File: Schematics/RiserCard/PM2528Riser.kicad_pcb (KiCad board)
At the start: 2 copper layers, 116.5 x 105 mm, 64 parts, among them K2 Conn_02x40_Odd_Even

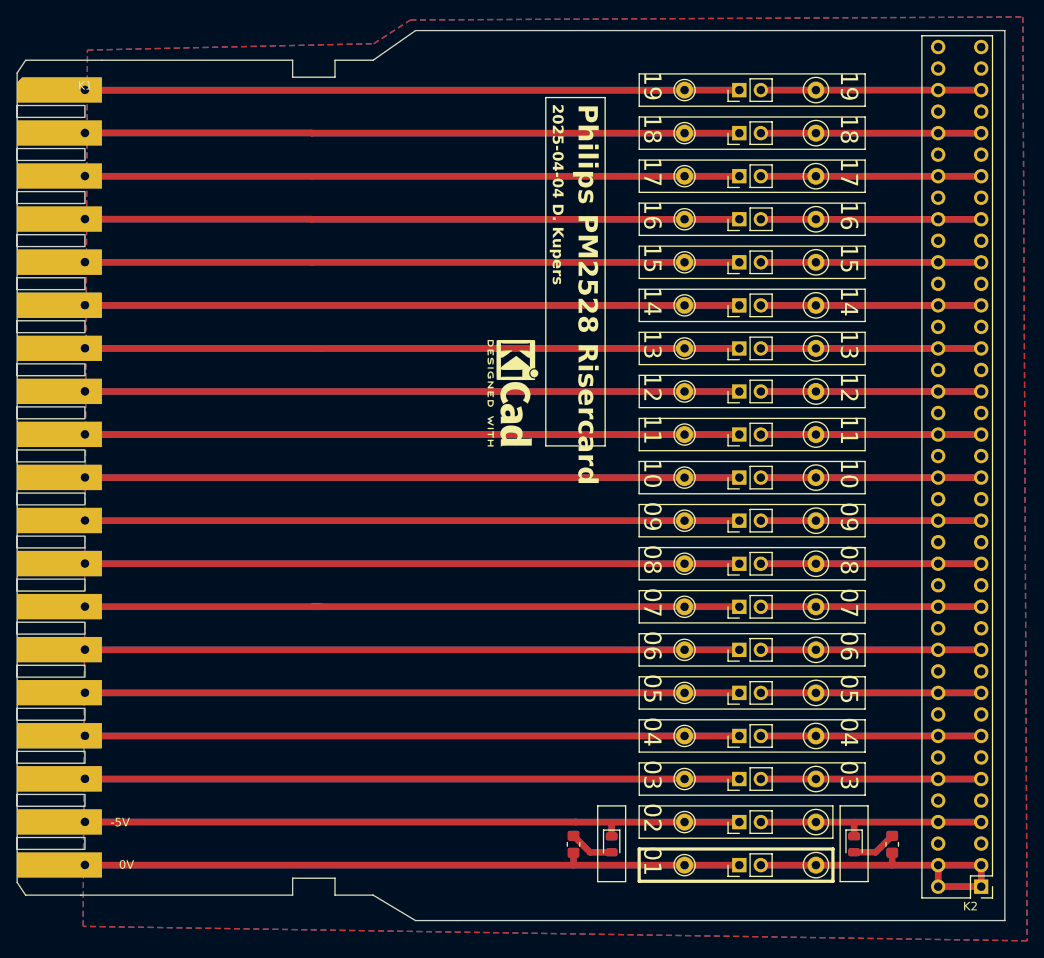
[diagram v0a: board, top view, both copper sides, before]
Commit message: Reworked N20/N21
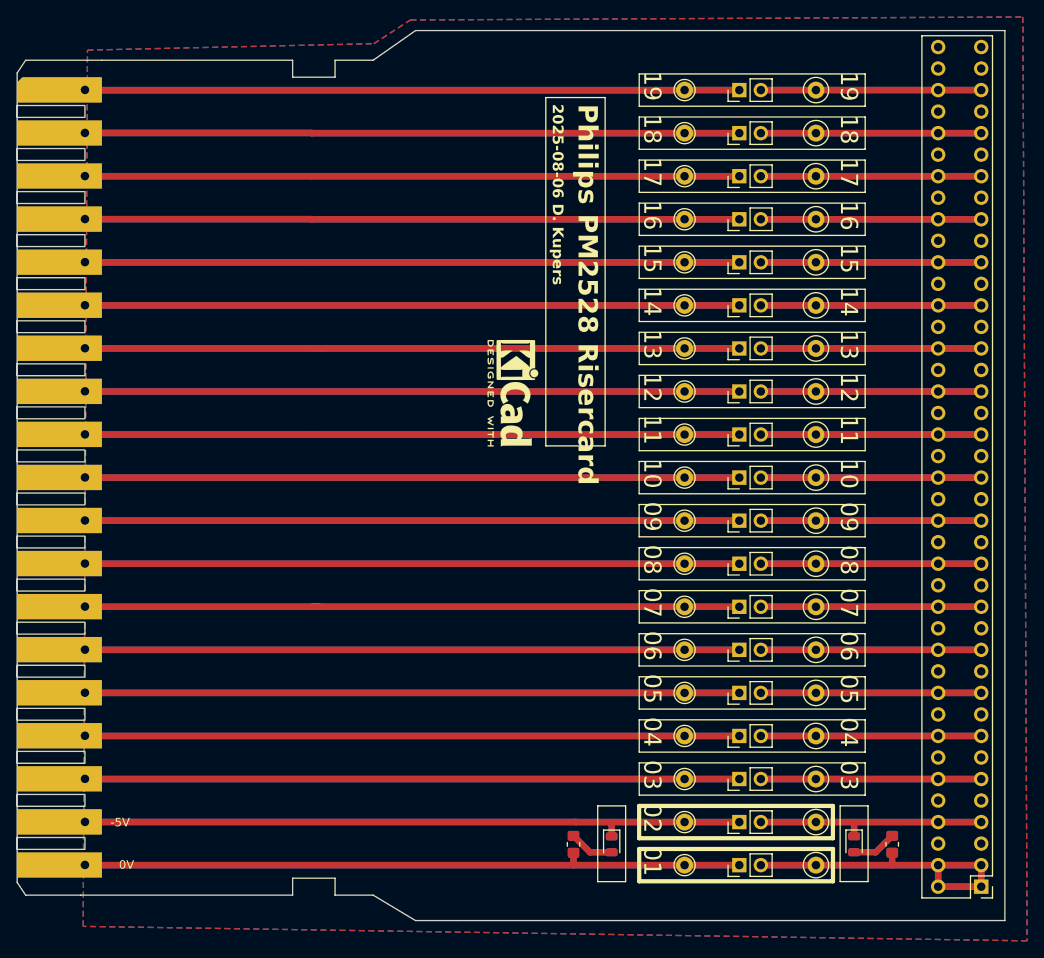
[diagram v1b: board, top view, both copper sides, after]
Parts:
- R1, R2: value 200 -> 470
- renumbered K2 to XRiser-2, K1 to XRiser01
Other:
- board text added: "2025-08-06 D. Kupers"
- board text removed: "2025-04-04 D. Kupers"
